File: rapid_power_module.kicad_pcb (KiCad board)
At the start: 2 copper layers, 101.5 x 84 mm, 191 parts, among them J1 Keystone 1048, J10 SWD Header, J11 SWD Header, J12 SWD Header, J2 Molex MicroFit 2x3, J3 Molex MicroFit 2x2, J4 Molex MicroFit 2x2, J5 Molex MicroFit 2x2, J6 Molex MicroFit 2x2, J7 Molex MicroFit 2x3, J8 Molex MicroFit 2x3, J9 Molex MicroFit 2x3, SW1 KMR721NGLFS, SW2 KMR721NGLFS, U1 STM32F042F6Px, U10 L7805, U11 MCP2562-E-SN, U12 STM32F105RCTx, U13 AZ1117I-3.3, U2 L7805, U3 AZ1117I-3.3, U4 BQ25171-Q1, U5 BQ29200, U6 MCP2562-E-SN, U7 INA213, U8 BQ25750RRVR, U9 BQ76952PFBR, Y1 8MHz, 12p, Y3 8MHz 12pF

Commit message: update parts
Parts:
- removed C1: 470n, Capacitor_SMD:C_0603_1608Metric
- removed C10, C9: 10p, Capacitor_SMD:C_0603_1608Metric
- removed C11, C14, C15, C16, C17, C18, C19, C2, C20, C6, C8: 100n, Capacitor_SMD:C_0603_1608Metric
- removed C12, C13, C7: 1u, Capacitor_SMD:C_0805_2012Metric
- removed C21, C22, C23, C24, C25, C26, C27, C28: 47u, Capacitor_SMD:C_1206_3216Metric
- removed C3, C5: 10u, Capacitor_SMD:C_1206_3216Metric
- removed C4: 22u, Capacitor_SMD:C_1206_3216Metric
- removed D1: ~, Diode_SMD:D_SMA
- removed D2: yellow, LED_SMD:LED_0603_1608Metric
- removed D3: red, LED_SMD:LED_0603_1608Metric
- removed D5, D6: 3V9, ZenerDiode:SOD323F_DIO
- removed F1: 1.5A, Fuse:Fuse_1206_3216Metric
- removed J1: Keystone 1048, frodo_power_module:keystone_1048
- removed J10: SWD Header, Connector_PinHeader_2.54mm:PinHeader_1x04_P2.54mm_Vertical
- removed J2, J7: Molex MicroFit 2x3, Connector_Molex:Molex_Micro-Fit_3.0_43045-0600_2x03_P3.00mm_Horizontal
- removed J3, J4: Molex MicroFit 2x2, Connector_Molex:Molex_Micro-Fit_3.0_43045-0400_2x02_P3.00mm_Horizontal
- removed JP1: r, Jumper:SolderJumper-2_P1.3mm_Open_RoundedPad1.0x1.5mm
- removed L1: BEAD, Inductor_SMD:L_0603_1608Metric
- removed R1: 120, DNP, Resistor_SMD:R_0603_1608Metric
- removed R10: 0, Resistor_SMD:R_0603_1608Metric
- removed R13: 5m, Resistor_SMD:R_2512_6332Metric
- removed R14, R17: 100, Resistor_SMD:R_0603_1608Metric
- removed R15: 120, Resistor_SMD:R_0603_1608Metric
- removed R16: 220, Resistor_SMD:R_0603_1608Metric
- removed R18, R19, R4: 10k, Resistor_SMD:R_0603_1608Metric
- removed R20: 5k1, Resistor_SMD:R_0603_1608Metric
- removed R21, R23, R3, R7: 1k, Resistor_SMD:R_0603_1608Metric
- removed R22, R24, R6: 1k8, Resistor_SMD:R_0603_1608Metric
- removed R25, R26: 1k5, Resistor_SMD:R_0603_1608Metric
- removed R27, R28: 22k, Resistor_SMD:R_0603_1608Metric
- removed R5: 100k, Resistor_SMD:R_0603_1608Metric
- removed R8: 680, Resistor_SMD:R_0603_1608Metric
- removed R9: DNP, Resistor_SMD:R_0603_1608Metric
- removed TH1: NCU18XH103F6SRB, Resistor_SMD:R_0603_1608Metric
- removed U1: STM32F042F6Px, Package_SO:TSSOP-20_4.4x6.5mm_P0.65mm
- removed U2: L7805, Package_TO_SOT_SMD:TO-252-2
- removed U3: AZ1117I-3.3, Package_TO_SOT_SMD:SOT-223-3_TabPin2
- removed U4: BQ25171-Q1, Package_SON:Texas_S-PVSON-N10_ThermalVias
- removed U5: BQ29200, Package_SON:Texas_S-PVSON-N8_ThermalVias
- removed U6: MCP2562-E-SN, Package_SO:SOIC-8_3.9x4.9mm_P1.27mm
- removed U7: INA213, Package_TO_SOT_SMD:SOT-363_SC-70-6
- removed U8: BQ25750RRVR, bq25750:VQFN36_RRV_TEX
- removed U9: BQ76952PFBR, bq76952:QFP_2PFBR_TEX
- removed Y1: 8MHz, 12p, Crystal:Crystal_SMD_5032-4Pin_5.0x3.2mm
- moved U10 83.7 mm to (67.7, 57.4)
- moved C67 80.5 mm to (62.2, 62.4)
- moved C68 80.5 mm to (62.2, 64.3)
- moved C69 80.5 mm to (62.2, 66.3)
- moved C70 80.5 mm to (62.2, 68.3)
- moved C71 80.5 mm to (62.2, 70.2)
- moved C72 80.5 mm to (65.1, 62.4)
- moved C73 80.5 mm to (65.1, 64.3)
- moved C74 80.5 mm to (65.1, 66.3)
- moved C75 80.5 mm to (65.1, 68.3)
- moved C76 80.5 mm to (65.1, 70.2)
- moved C77 80.5 mm to (68.0, 62.4)
- moved C78 80.5 mm to (68.0, 64.3)
- moved C79 80.5 mm to (68.0, 66.3)
- moved U13 76.3 mm to (65.7, 75.4)
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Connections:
- H1 pad 1: GND -> 1N
- H2 pad 1: GND -> 1N
- H3 pad 1: GND -> 1N
- H4 pad 1: GND -> 1N

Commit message: added some footprints
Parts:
- added BT1: Battery_Cell, Inductor Wuerth:BAT_1043, F.Cu at (200.5, 37.2)
- added BT2: Battery_Cell, Inductor Wuerth:BAT_1043, F.Cu at (200.0, 60.0)
- added BT3: Battery_Cell, Inductor Wuerth:BAT_1043, F.Cu at (200.0, 82.2)
- added C1: 470n, Capacitor_SMD:C_0603_1608Metric, F.Cu at (124.8, 67.4)
- added C2: 82u, Capacitor_SMD:C_0603_1608Metric, F.Cu at (124.8, 69.9)
- added C23: 3u3, Capacitor_SMD:C_0402_1005Metric, F.Cu at (118.0, 60.0)
- added C3: 100n, Capacitor_SMD:C_0603_1608Metric, F.Cu at (124.8, 72.4)
- added C4: 174u, Capacitor_SMD:C_0603_1608Metric, F.Cu at (124.8, 74.9)
- added C5: 82u, Capacitor_SMD:C_0603_1608Metric, F.Cu at (124.8, 77.4)
- added C59: 100n, Capacitor_SMD:C_0402_1005Metric, F.Cu at (118.0, 62.0)
- added C6: 174u, Capacitor_SMD:C_0603_1608Metric, F.Cu at (124.8, 80.0)
- added C65: 1u, Capacitor_SMD:C_0603_1608Metric, F.Cu at (128.9, 72.4)
- added C7: 10u, Capacitor_SMD:C_0603_1608Metric, F.Cu at (128.9, 67.4)
- added C8: 10u, Capacitor_SMD:C_0603_1608Metric, F.Cu at (128.9, 69.9)
- added C81: 100n, Capacitor_SMD:C_0402_1005Metric, F.Cu at (118.0, 63.9)
- added C82: 10u, Capacitor_SMD:C_0603_1608Metric, F.Cu at (128.9, 74.9)
- added C83: 10n, Capacitor_SMD:C_0402_1005Metric, F.Cu at (118.0, 65.9)
- added C84: 10u, Capacitor_SMD:C_0603_1608Metric, F.Cu at (128.9, 77.4)
- added C85: 10n, Capacitor_SMD:C_0402_1005Metric, F.Cu at (118.0, 67.9)
- added C86: 10u, Capacitor_SMD:C_0603_1608Metric, F.Cu at (128.9, 80.0)
- added C87: 10n, Capacitor_SMD:C_0402_1005Metric, F.Cu at (118.0, 69.8)
- added C88: 10u, Capacitor_SMD:C_0603_1608Metric, F.Cu at (132.9, 67.4)
- added C89: 10n, Capacitor_SMD:C_0402_1005Metric, F.Cu at (118.0, 71.8)
- added C90: 10u, Capacitor_SMD:C_0603_1608Metric, F.Cu at (132.9, 69.9)
- added C91: 10n, Capacitor_SMD:C_0402_1005Metric, F.Cu at (118.0, 73.8)
- added D1: ~, Diode_SMD:ST_D_SMC, F.Cu at (91.6, 25.7)
- added D16: green, LED_SMD:LED_0603_1608Metric, F.Cu at (143.1, 43.2)
- added D17: red, LED_SMD:LED_0603_1608Metric, F.Cu at (143.1, 45.8)
- added D18: yellow, LED_SMD:LED_0603_1608Metric, F.Cu at (143.1, 48.4)
- added D19: green, LED_SMD:LED_0603_1608Metric, F.Cu at (147.2, 38.0)
- added D2: ~, Diode_SMD:ST_D_SMC, F.Cu at (91.6, 33.2)
- added D20: yellow, LED_SMD:LED_0603_1608Metric, F.Cu at (147.2, 40.6)
- added D21: green, LED_SMD:LED_0603_1608Metric, F.Cu at (147.2, 43.2)
- added D22: red, LED_SMD:LED_0603_1608Metric, F.Cu at (147.2, 45.8)
- added D23: green, LED_SMD:LED_0603_1608Metric, F.Cu at (147.2, 48.4)
- added D24: Vz = 3.6V, Diode_SMD:Nexperia_CFP3_SOD-123W, F.Cu at (119.4, 76.4)
- added D3: ~, Diode_SMD:ST_D_SMC, F.Cu at (91.6, 40.6)
- added D4: ~, Diode_SMD:ST_D_SMC, F.Cu at (91.6, 48.1)
- added D5: green, LED_SMD:LED_0603_1608Metric, F.Cu at (143.1, 38.0)
- added D6: ~, Diode_SMD:ST_D_SMC, F.Cu at (91.6, 55.5)
- added D7: green, LED_SMD:LED_0603_1608Metric, F.Cu at (143.1, 40.6)
- added D8: ~, Diode_SMD:ST_D_SMC, F.Cu at (91.6, 63.0)
- added F1: 3A, Fuse:Fuseholder_Cylinder-5x20mm_Wuerth_696103101002-SMD_Horizontal_Open, F.Cu at (109.7, 42.3)
- added F3: 10A, Fuse:Fuseholder_Cylinder-5x20mm_Wuerth_696103101002-SMD_Horizontal_Open, F.Cu at (109.7, 53.4)
- added FB2: 120R, Inductor_SMD:L_0805_2012Metric, F.Cu at (88.9, 74.4)
- added FB3: 120R, Inductor_SMD:L_0805_2012Metric, F.Cu at (88.9, 77.1)
- added J1: Conn_02x04_Top_Bottom, Connector_Molex:Molex_Micro-Fit_3.0_43045-0800_2x04_P3.00mm_Horizontal, F.Cu at (127.5, 46.6)
- added J16: USB_C_Receptacle_USB2.0, Connector_USB:USB_C_Receptacle_Palconn_UTC16-G, F.Cu at (144.7, 70.3)
- added J17: TC2050, Connector:Tag-Connect_TC2050-IDC-FP_2x05_P1.27mm_Vertical, F.Cu at (139.2, 26.8)
- added J3: Conn_02x04_Top_Bottom, Connector_Molex:Molex_Micro-Fit_3.0_43045-0800_2x04_P3.00mm_Horizontal, F.Cu at (127.5, 61.4)
- added J7: Molex MicroFit 2x2, Connector_Molex:Molex_Micro-Fit_3.0_43045-0400_2x02_P3.00mm_Horizontal, F.Cu at (101.1, 31.9)
- added J8: Molex MicroFit 2x2, Connector_Molex:Molex_Micro-Fit_3.0_43045-0400_2x02_P3.00mm_Horizontal, F.Cu at (113.3, 31.9)
- added J9: Molex MicroFit 2x2, Connector_Molex:Molex_Micro-Fit_3.0_43045-0400_2x02_P3.00mm_Horizontal, F.Cu at (125.5, 31.9)
- added L2: 5u6, Inductor Wuerth:Wuerth 7443557560, F.Cu at (260.5, 36.5)
- added R1: 10, Resistor_SMD:R_0603_1608Metric, F.Cu at (132.9, 72.4)
- added R14: 1k, Resistor_SMD:R_0402_1005Metric, F.Cu at (142.5, 50.6)
- added R15: 1k, Resistor_SMD:R_0402_1005Metric, F.Cu at (142.5, 52.6)
- added R16: 1k, Resistor_SMD:R_0402_1005Metric, F.Cu at (142.5, 54.6)
- added R17: 1k, Resistor_SMD:R_0402_1005Metric, F.Cu at (142.5, 56.6)
- added R26: 1k, Resistor_SMD:R_0402_1005Metric, F.Cu at (142.5, 58.6)
- added R3: 35k, Resistor_SMD:R_0603_1608Metric, F.Cu at (132.9, 74.9)
- added R45: 4k7, Resistor_SMD:R_0402_1005Metric, F.Cu at (142.5, 60.6)
- added R73: 22R, Resistor_SMD:R_0402_1005Metric, F.Cu at (145.4, 50.6)
- added R75: 22R, Resistor_SMD:R_0402_1005Metric, F.Cu at (145.4, 52.6)
- added R86: 22, Resistor_SMD:R_0402_1005Metric, F.Cu at (145.4, 54.6)
- added R87: 22, Resistor_SMD:R_0402_1005Metric, F.Cu at (145.4, 56.6)
- added R88: 22, Resistor_SMD:R_0402_1005Metric, F.Cu at (145.4, 58.6)
- added R89: 1k, Resistor_SMD:R_0402_1005Metric, F.Cu at (145.4, 60.6)
- added R90: 1k, Resistor_SMD:R_0402_1005Metric, F.Cu at (148.3, 50.6)
- added R91: 10k, Resistor_SMD:R_0603_1608Metric, F.Cu at (132.9, 77.4)
- added R92: 0R, Resistor_SMD:R_0402_1005Metric, F.Cu at (148.3, 52.6)
- added R93: 0R, Resistor_SMD:R_0402_1005Metric, F.Cu at (148.3, 54.6)
- added R94: 16k, Resistor_SMD:R_0603_1608Metric, F.Cu at (132.9, 80.0)
- added R95: 8k, Resistor_SMD:R_0603_1608Metric, F.Cu at (136.9, 67.4)
- added R96: 4k, Resistor_SMD:R_0603_1608Metric, F.Cu at (136.9, 69.9)
- added R97: 20k, Resistor_SMD:R_0603_1608Metric, F.Cu at (136.9, 72.4)
- added R98: 12.5k, Resistor_SMD:R_0603_1608Metric, F.Cu at (136.9, 74.9)
- added U14: TPD4E1U06, Package_TO_SOT_SMD:SOT-563, F.Cu at (93.4, 74.5)
- added U15: TPD4E1U06, Package_TO_SOT_SMD:SOT-563, F.Cu at (93.4, 77.5)
- added U2: CYPD3177-24LQ, Package_DFN_QFN:QFN-24-1EP_4x4mm_P0.5mm_EP2.75x2.75mm, F.Cu at (89.8, 69.8)
- R31: value 80k -> 50k
- R32: value 5k24 -> 4k5
- R33: value 6k26 -> 310k
- R43: value 22k1 -> 65k
- R44: value 1k -> 1000k
- R82: value 30k31 -> 22k5
- R83: value 4k2 -> 50k
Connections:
- net Net-(U8-SRN) renamed SRP
- net Net-(U8-SRP) renamed SRN
- C37 pad 1: 1N -> ISNK_FINE
- C38 pad 2: 1N -> ISNK_FINE
- C44 pad 2: 1N -> ISNK_FINE
- C45 pad 1: 1N -> ISNK_FINE
- C47 pad 2: 1N -> ISNK_FINE
- C48 pad 2: 1N -> ISNK_FINE
- C58 pad 1: 1N -> ISNK_FINE
- C58 pad 2: +VSW -> Net-(U10-IN)
- C60 pad 2: 1N -> ISNK_FINE
- C61 pad 1: 1N -> ISNK_FINE
- C62 pad 2: 1N -> ISNK_FINE
- C67 pad 2: 1N -> ISNK_FINE
- C68 pad 2: 1N -> ISNK_FINE
- C69 pad 2: 1N -> ISNK_FINE
- C70 pad 2: 1N -> ISNK_FINE
- C71 pad 2: 1N -> ISNK_FINE
- C72 pad 2: 1N -> ISNK_FINE
- C73 pad 2: 1N -> ISNK_FINE
- C74 pad 2: 1N -> ISNK_FINE
- C75 pad 2: 1N -> ISNK_FINE
- C76 pad 2: 1N -> ISNK_FINE
- C77 pad 2: 1N -> ISNK_FINE
- C78 pad 2: 1N -> ISNK_FINE
- C79 pad 1: 1N -> ISNK_FINE
- C80 pad 1: 1N -> ISNK_FINE
- H1 pad 1: 1N -> ISNK_FINE
- H2 pad 1: 1N -> ISNK_FINE
- H3 pad 1: 1N -> ISNK_FINE
- H4 pad 1: 1N -> ISNK_FINE
- J11 pad 4: 1N -> ISNK_FINE
- J12 pad 4: 1N -> ISNK_FINE
- J5 pad 3: PRE_OUT -> Net-(J5-Pin_3)
- J5 pad 4: PRE_OUT -> Net-(J5-Pin_3)
- J6 pad 1: 1N -> ISNK_FINE
- J6 pad 2: 1N -> ISNK_FINE
- R31 pad 2: 1N -> ISNK_FINE
- R32 pad 1: 1N -> Net-(U1-TS)
- R36 pad 1: Net-(Q4-D) -> Net-(U1-FB)
- R36 pad 2: 3P -> PACK+
- R37 pad 2: Net-(R37-Pad2) -> PACK+
- R41 pad 2: 3P -> Net-(Q8-D)
- R43 pad 2: 1N -> ISNK_FINE
- R69 pad 2: PG -> Net-(D22-A)
- R76 pad 1: 1N -> ISNK_FINE
- R79 pad 1: PRE_OUT -> Net-(Q5-D)
- R80 pad 1: Net-(Q2-D) -> VAC
- R82 pad 1: 1N -> Net-(U1-TS)
- R82 pad 2: 1N -> ISNK_FINE
- R83 pad 2: 1N -> ISNK_FINE
- SW2 pad 1: 1N -> ISNK_FINE
- U10 pad 1: +VSW -> Net-(U10-IN)
- U10 pad 2: 1N -> ISNK_FINE
- U11 pad 2: 1N -> ISNK_FINE
- U11 pad 8: 1N -> ISNK_FINE
- U12 pad 12: 1N -> ISNK_FINE
- U12 pad 18: 1N -> ISNK_FINE
- U12 pad 2: unconnected-(U12-PC13-Pad2) -> STAT_LED0
- U12 pad 21: unconnected-(U12-PA5-Pad21) -> USB_PD_INTERRUPT
- U12 pad 24: ALERT -> BAL_ALERT
- U12 pad 3: unconnected-(U12-PC14-Pad3) -> STAT_LED1
- U12 pad 31: 1N -> ISNK_FINE
- U12 pad 33: unconnected-(U12-PB12-Pad33) -> CHRG_IND_LED_1
- U12 pad 34: unconnected-(U12-PB13-Pad34) -> CHRG_IND_LED_2
- U12 pad 35: unconnected-(U12-PB14-Pad35) -> CHRG_IND_LED_3
- U12 pad 36: unconnected-(U12-PB15-Pad36) -> CHRG_IND_LED_4
- U12 pad 4: unconnected-(U12-PC15-Pad4) -> STAT_LED2
- U12 pad 40: unconnected-(U12-PC9-Pad40) -> CE
- U12 pad 42: unconnected-(U12-PA9-Pad42) -> USB_FS_VBUS
- U12 pad 44: CAN_RX -> USB_D-
- U12 pad 45: CAN_TX -> USB_D+
- U12 pad 47: 1N -> ISNK_FINE
- U12 pad 50: unconnected-(U12-PA15-Pad50) -> SWO
- U12 pad 58: unconnected-(U12-PB6-Pad58) -> I2C_SCL
- U12 pad 59: unconnected-(U12-PB7-Pad59) -> I2C_SDA
- U12 pad 61: I2C_SCL -> CAN_RX
- U12 pad 62: I2C_SDA -> CAN_TX
- U12 pad 63: 1N -> ISNK_FINE
- U13 pad 1: 1N -> ISNK_FINE
- Y3 pad 2: 1N -> ISNK_FINE
- Y3 pad 4: 1N -> ISNK_FINE
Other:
- board size 101.5 x 84 mm -> 129 x 131.5 mm

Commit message: Added Testpoints and some LCSC numbers
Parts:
- removed C29, C30, C31, C32: 220n, Capacitor_SMD:C_0603_1608Metric
- removed C33: 1u, Capacitor_SMD:C_1206_3216Metric
- removed C34, C63: 100p, Capacitor_SMD:C_0603_1608Metric
- removed C35: 470n, Capacitor_SMD:C_0603_1608Metric
- removed C36, C50, C51, C55, C56, C64: 100n, Capacitor_SMD:C_0603_1608Metric
- removed C40: 2u2, Capacitor_SMD:C_1206_3216Metric
- removed C41, C42: 80u, Capacitor_SMD:C_1206_3216Metric
- removed C52: 22n, Capacitor_SMD:C_0603_1608Metric
- removed C53, C54: 1uF, Capacitor_SMD:C_1206_3216Metric
- removed C57: 2.2u, Capacitor_SMD:C_1206_3216Metric
- removed D8: ~, Diode_SMD:ST_D_SMC
- removed the J8 at (65.0, 33.0)
- removed the J9 at (65.0, 47.7)
- removed R1: 10, Resistor_SMD:R_0603_1608Metric
- removed R29: 20, Resistor_SMD:R_0603_1608Metric
- removed R30, R71, R78: 100, Resistor_SMD:R_0603_1608Metric
- removed R39, R46, R53: 7k5, Resistor_SMD:R_0603_1608Metric
- removed R40: 3k3, Resistor_SMD:R_0603_1608Metric
- removed R42: 12k, Resistor_SMD:R_0603_1608Metric
- removed R47: 20k, Resistor_SMD:R_0603_1608Metric
- removed R48, R50, R59, R60, R61, R62: 5.1k, Resistor_SMD:R_0603_1608Metric
- removed R51: 0, Resistor_SMD:R_0603_1608Metric
- removed R52, R54: 5k1, Resistor_SMD:R_0603_1608Metric
- removed R68: 4k7, Resistor_SMD:R_0603_1608Metric
- removed R77: 0.001, Resistor_SMD:R_0603_1608Metric
- removed R81: 2, Resistor_SMD:R_0603_1608Metric
- added C10: 1u, Capacitor_SMD:C_0805_2012Metric, F.Cu at (97.0, 111.0)
- added C11: 1u, Capacitor_SMD:C_0805_2012Metric, F.Cu at (97.0, 114.0)
- added C12: 100n, Capacitor_SMD:C_0603_1608Metric, F.Cu at (84.8, 110.2)
- added C13: 100n, Capacitor_SMD:C_0603_1608Metric, F.Cu at (84.8, 112.7)
- added C14: 220n, Capacitor_SMD:C_0603_1608Metric, F.Cu at (84.8, 115.2)
- added C15: 220n, Capacitor_SMD:C_0603_1608Metric, F.Cu at (84.8, 117.8)
- added C16: 220n, Capacitor_SMD:C_0603_1608Metric, F.Cu at (84.8, 120.3)
- added C17: 220n, Capacitor_SMD:C_0603_1608Metric, F.Cu at (84.8, 122.8)
- added C18: 470n, Capacitor_SMD:C_0603_1608Metric, F.Cu at (88.8, 107.7)
- added C19: 1u, Capacitor_SMD:C_0805_2012Metric, F.Cu at (97.0, 117.0)
- added C21: 2u2, Capacitor_SMD:C_0805_2012Metric, F.Cu at (97.0, 120.0)
- added C24: 100p, Capacitor_SMD:C_0603_1608Metric, F.Cu at (88.8, 110.2)
- added C9: 1u, Capacitor_SMD:C_0805_2012Metric, F.Cu at (97.0, 108.0)
- added R10: 5k1, Resistor_SMD:R_0603_1608Metric, F.Cu at (92.8, 110.2)
- added R13: 10k, Resistor_SMD:R_0603_1608Metric, F.Cu at (92.8, 112.7)
- added R18: 5k1, Resistor_SMD:R_0603_1608Metric, F.Cu at (92.8, 115.2)
- added R19: 5k1, Resistor_SMD:R_0603_1608Metric, F.Cu at (92.8, 117.8)
- added R2: 20, Resistor_SMD:R_2512_6332Metric, F.Cu at (78.4, 108.9)
- added R20: 20, Resistor_SMD:R_2512_6332Metric, F.Cu at (78.4, 123.6)
- added R21: 100, Resistor_SMD:R_2512_6332Metric, F.Cu at (78.4, 128.6)
- added R23: 4k7, Resistor_SMD:R_0603_1608Metric, F.Cu at (92.8, 120.3)
- added R24: 100k, Resistor_SMD:R_0603_1608Metric, F.Cu at (92.8, 122.8)
- added R4: 10k, Resistor_SMD:R_0603_1608Metric, F.Cu at (88.8, 112.7)
- added R5: 1k, Resistor_SMD:R_0603_1608Metric, F.Cu at (88.8, 115.2)
- added R6: 5k1, Resistor_SMD:R_0603_1608Metric, F.Cu at (88.8, 117.8)
- added R7: 5k1, Resistor_SMD:R_0603_1608Metric, F.Cu at (88.8, 120.3)
- added R8: 49k9, Resistor_SMD:R_0603_1608Metric, F.Cu at (88.8, 122.8)
- added R9: 1k, Resistor_SMD:R_0603_1608Metric, F.Cu at (92.8, 107.7)
- added U1: BQ25756RRVR, Package_DFN_QFN:Texas_RHH0036C_VQFN-36-1EP_6x6mm_P0.5mm_EP4.4x4.4mm, F.Cu at (226.6, 42.0)
- added U3: BQ76952PFBR, Package_QFP:TQFP-48_7x7mm_P0.5mm, F.Cu at (214.5, 86.0)
- BT1, BT2, BT3, F1, F3, J16, J7, J8, J9: moved to B.Cu
- C1: value 470n -> 100n
- R11, R12: footprint Capacitor_SMD:C_0603_1608Metric -> Resistor_SMD:R_2512_6332Metric
- R14, R15, R16, R17: footprint Resistor_SMD:R_0402_1005Metric -> Resistor_SMD:R_0603_1608Metric
- R44: footprint Resistor_SMD:R_0603_1608Metric -> Resistor_SMD:R_0805_2012Metric
- moved H4 233.1 mm to (252.3, 128.3)
- moved H2 227.7 mm to (260.0, 40.0)
- moved J5 211.1 mm to (243.0, 124.2), turned to 180 degrees
- moved J11 189.9 mm to (240.4, 38.7)
- moved J12 189.9 mm to (245.0, 38.7)
- moved J6 188.5 mm to (231.5, 124.2), turned to 180 degrees
- moved U12 188.4 mm to (231.8, 85.3)
- moved H3 173.9 mm to (184.6, 127.0)
- moved F3 163.7 mm to (267.0, 98.5), turned to 90 degrees
- moved F1 160.0 mm to (267.0, 71.5), turned to -90 degrees
- moved H1 148.2 mm to (180.0, 40.0)
- moved J7 130.6 mm to (193.5, 124.2)
- moved J8 130.4 mm to (205.5, 124.2)
- moved J9 129.9 mm to (217.0, 124.2)
- moved J3 118.8 mm to (241.0, 26.5)
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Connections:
- net Net-(Q8-D) renamed BuckBoostOut
- R11 pad 2: 2P -> CELL 2
- R12 pad 2: 1P -> CELL 1
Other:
- board size 129 x 131.5 mm -> 110.8 x 136 mm

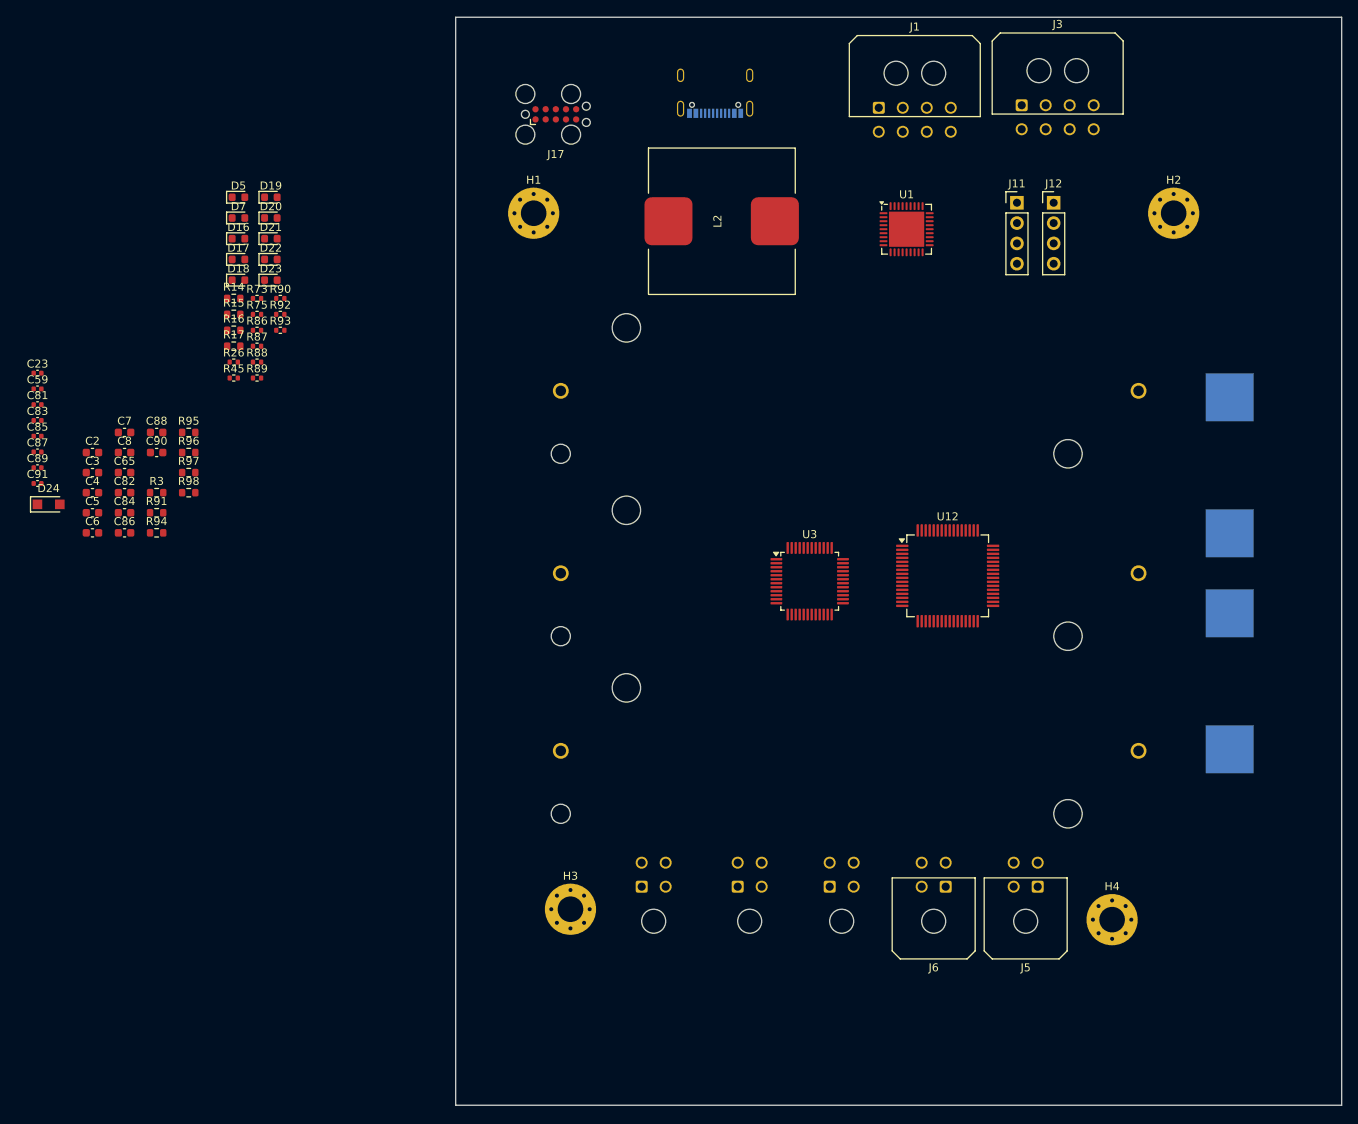
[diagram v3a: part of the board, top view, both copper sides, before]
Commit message: Routing for 4 pin connectors
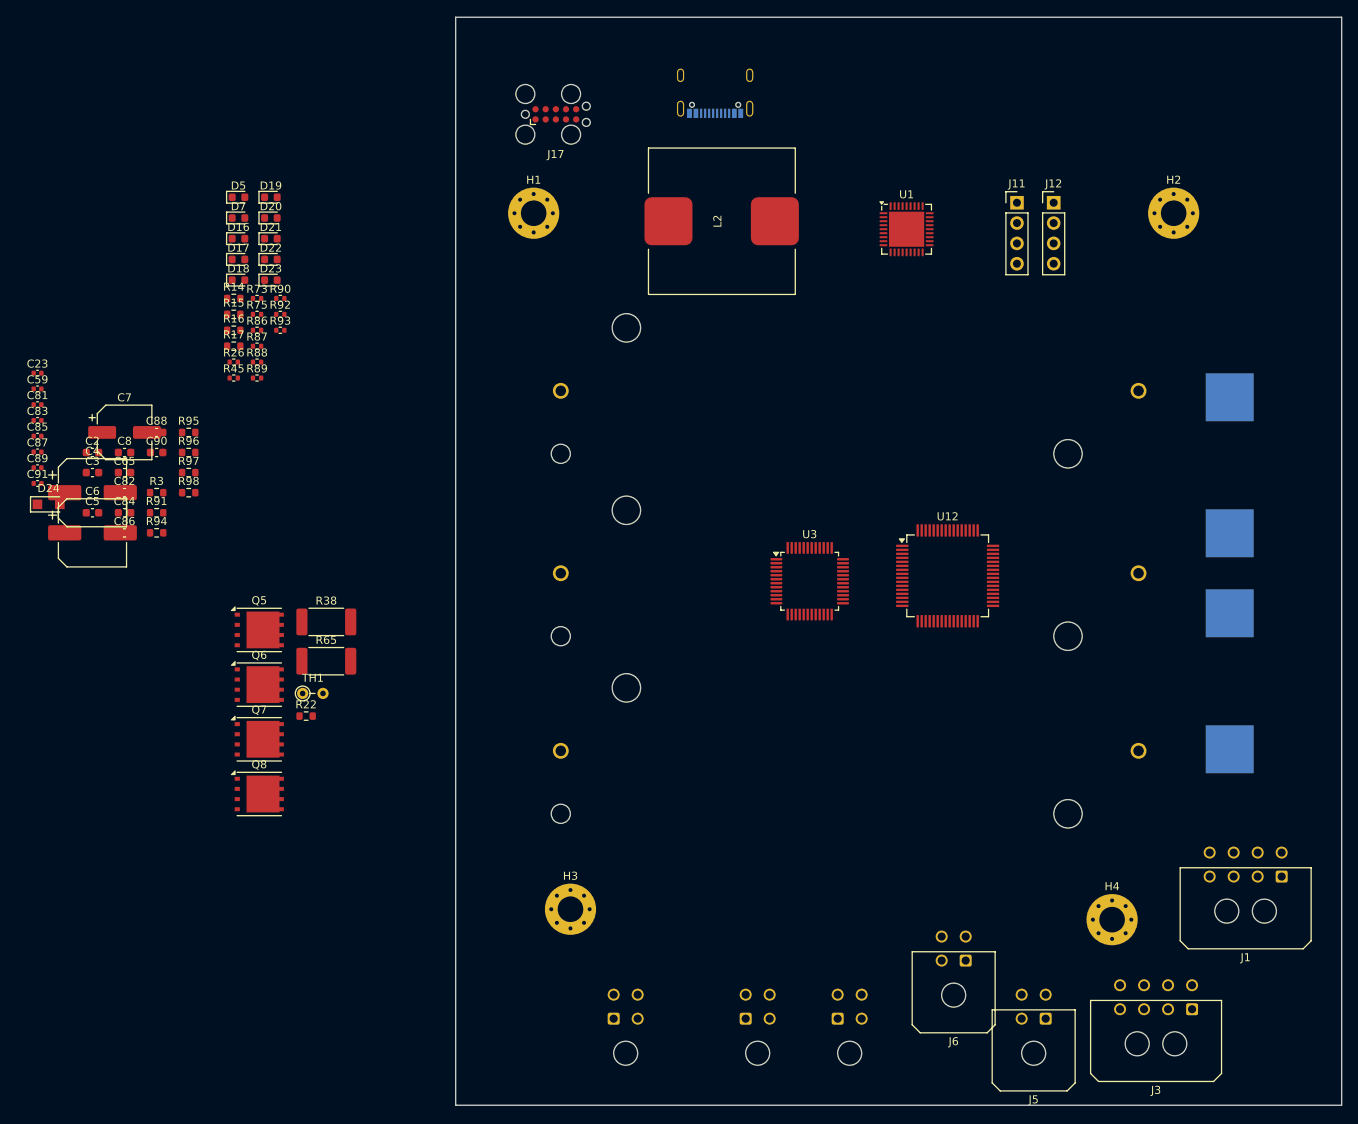
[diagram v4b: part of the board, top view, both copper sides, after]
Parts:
- added Q5: NMOS, Package_DFN_QFN:AO_DFN-8-1EP_5.55x5.2mm_P1.27mm_EP4.12x4.6mm, F.Cu at (145.7, 92.1)
- added Q6: NMOS, Package_DFN_QFN:AO_DFN-8-1EP_5.55x5.2mm_P1.27mm_EP4.12x4.6mm, F.Cu at (145.7, 98.9)
- added Q7: NMOS, Package_DFN_QFN:AO_DFN-8-1EP_5.55x5.2mm_P1.27mm_EP4.12x4.6mm, F.Cu at (145.7, 105.8)
- added Q8: NMOS, Package_DFN_QFN:AO_DFN-8-1EP_5.55x5.2mm_P1.27mm_EP4.12x4.6mm, F.Cu at (145.7, 112.6)
- added R22: 10, Resistor_SMD:R_0603_1608Metric, F.Cu at (151.6, 102.9)
- added R38: 5m, Resistor_SMD:R_2512_6332Metric_Pad1.40x3.35mm_HandSolder, F.Cu at (154.1, 91.1)
- added R65: 5m, Resistor_SMD:R_2512_6332Metric_Pad1.40x3.35mm_HandSolder, F.Cu at (154.1, 96.0)
- added TH1: Thermistor_NTC, Resistor_THT:R_Axial_DIN0204_L3.6mm_D1.6mm_P2.54mm_Vertical, F.Cu at (151.1, 100.0)
- C4, C6: footprint Capacitor_SMD:C_0603_1608Metric -> Capacitor_SMD:CP_Elec_8x6.9
- C7: footprint Capacitor_SMD:C_0603_1608Metric -> Capacitor_SMD:CP_Elec_6.3x5.9
- R33: value 310k -> 300k
- R43: value 65k -> 68k
- moved J3 115.0 mm to (262.3, 139.5), turned to 180 degrees
- moved J1 108.5 mm to (273.5, 122.9), turned to 180 degrees
- moved J7 16.9 mm to (190.0, 140.7)
- moved J5 16.5 mm to (244.0, 140.7)
- moved J8 16.5 mm to (206.5, 140.7)
- moved J9 16.5 mm to (218.0, 140.7)
- moved J6 9.57 mm to (234.0, 133.4)
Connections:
- C48 pad 1: +5V -> Net-(U1-DRV_SUP)
- R83 pad 1: Net-(J4-Pin_1) -> Net-(J4-Pin_2)
- R94 pad 1: Net-(J2-Pin_1) -> Net-(J2-Pin_2)
- U1 pad 23: +5V -> Net-(U1-DRV_SUP)
